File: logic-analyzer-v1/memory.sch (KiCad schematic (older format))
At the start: 12 parts

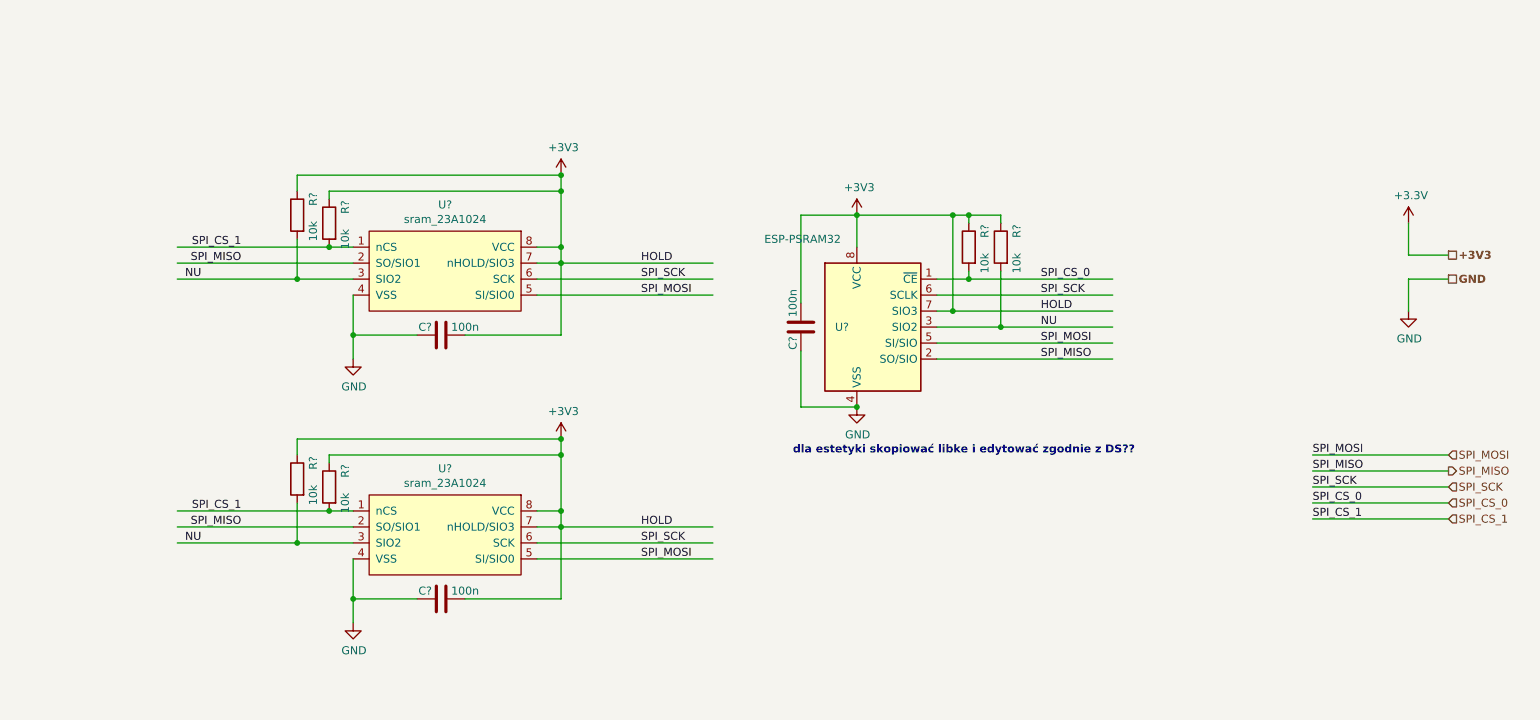
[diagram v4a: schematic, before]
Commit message: delete old sram
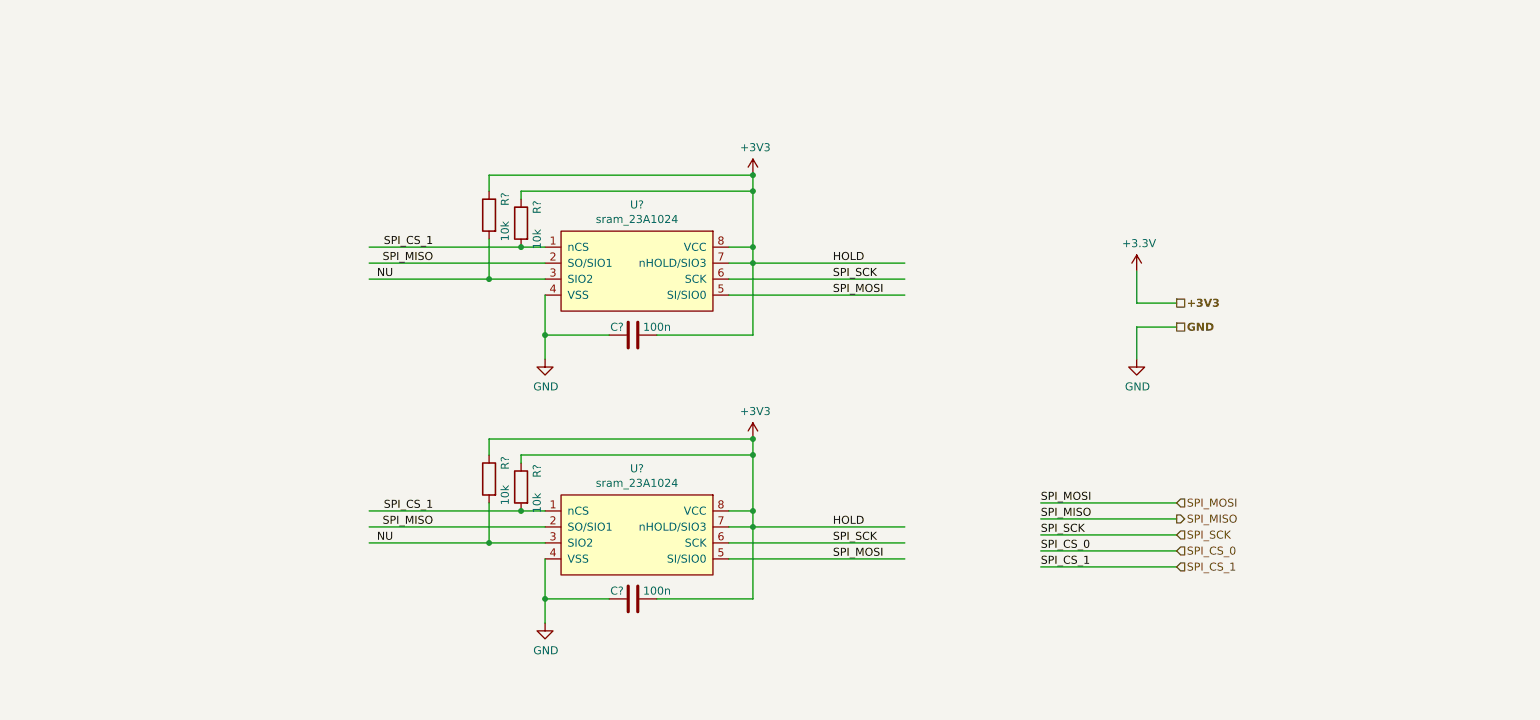
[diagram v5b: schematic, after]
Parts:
- removed C?: 100n, Capacitor_SMD:C_0603_1608Metric_Pad1.05x0.95mm_HandSolder, symbol Device:C
- removed R? (x2): 10k, Resistor_SMD:R_0603_1608Metric_Pad1.05x0.95mm_HandSolder, symbol Device:R
- removed U?: ESP-PSRAM32, Package_SO:SOIC-8_3.9x4.9mm_P1.27mm, symbol Memory_RAM:ESP-PSRAM32
- removed U?: sram_23A1024, symbol my_library:sram_23A1024
- added U?: sram_23A1024, Package_SO:SOIC-8_3.9x4.9mm_P1.27mm, symbol my_library:sram_23A1024
- U?: footprint (none) -> Package_SO:SOIC-8_3.9x4.9mm_P1.27mm
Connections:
- wire segments 77 -> 55
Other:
- note removed: "dla estetyki skopiować libke i edytować zgodnie z DS??"
- moved on the sheet: C?, R?, U?
